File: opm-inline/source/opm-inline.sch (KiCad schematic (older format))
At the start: 0 parts

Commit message: more value updates
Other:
- note removed: "Release history:"
- note removed: "• v1.0 - First release.\n• v1.1 - shunt amplifier to the smaller type.\n signals to connector remapped: AIN0 = ADC_I_u and\n AIN1 = ADC_I_w.\n I_v signal removed.\n• v1.2 - Added pullup resistor for EPROM."
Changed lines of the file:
@@
 Comment4 ""
 $EndDescr
-Text Notes 500  650  0    79   ~ 0
-Release history:
-Text Notes 500  1050 0    39   ~ 0
-• v1.0 - First release.\n• v1.1 - shunt amplifier to the smaller type.\n          signals to connector remapped: AIN0 = ADC_I_u and\n          AIN1 = ADC_I_w.\n          I_v signal removed.\n• v1.2 - Added pullup resistor for EPROM.
-Wire Notes Line
-	500  500  500  1500
-Wire Notes Line
-	500  1500 2500 1500
 $Sheet
 S 5500 1000 1000 2000
@@
 Text Label 3400 1850 2    39   ~ 0
 VCP
-Wire Notes Line
-	2500 500  500  500
-Wire Notes Line
-	2500 1500 2500 500
 $EndSCHEMATC

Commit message: remove regulator
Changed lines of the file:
@@
 $Descr A4 11693 8268
 encoding utf-8
-Sheet 1 4
+Sheet 1 3
 Title "TMC6100-EVAL"
 Date "2019-10-28"
@@
 F26 "VCP" O R 6500 2300 39
 $EndSheet
-$Sheet
-S 7500 1000 1000 1000
-U 5D6A7BED
-F0 "Regulator and ID" 39
-F1 "Regulator and ID.sch" 39
-F2 "+5V_VM" I L 7500 1100 39
-F3 "+Vcc_IO" O R 8500 1100 39
-F4 "Fault" I L 7500 1200 39
-F5 "~CS_EEPROM" I L 7500 1300 39
-F6 "SPI2_SCK" I L 7500 1400 39
-F7 "SPI2_MOSI" I L 7500 1500 39
-F8 "SPI2_MISO" O R 8500 1200 39
-F9 "+3,3V" O R 8500 1300 39
-$EndSheet
-Text Label 8600 1100 0    39   ~ 0
-+Vcc_IO
-Wire Wire Line
-	8600 1100 8500 1100
-Wire Wire Line
-	8500 1200 8600 1200
-Wire Wire Line
-	7500 1100 7400 1100
-Wire Wire Line
-	7400 1200 7500 1200
-Wire Wire Line
-	7400 1300 7500 1300
-Wire Wire Line
-	7400 1400 7500 1400
-Wire Wire Line
-	7400 1500 7500 1500
 Wire Wire Line
 	6600 1100 6500 1100
@@
 Text Label 3400 1500 2    39   ~ 0
 +Vcc_IO
-Text Label 7400 1100 2    39   ~ 0
-+5V_VM
 Text Label 5400 1300 2    39   ~ 0
 +5V_VM
@@
 ADC_I_w
 Text Label 6600 1700 0    39   ~ 0
-Fault
-Text Label 7400 1200 2    39   ~ 0
 Fault
 Text Label 4600 1700 0    39   ~ 0
@@
 Text Label 3400 1300 2    39   ~ 0
 ADC_I_w
-Text Label 7400 1300 2    39   ~ 0
-~CS_EEPROM
 Text Label 4600 2800 0    39   ~ 0
 ~CS_EEPROM
@@
 Text Label 5400 1800 2    39   ~ 0
 SPI2_MOSI
-Text Label 7400 1500 2    39   ~ 0
-SPI2_MOSI
-Text Label 7400 1400 2    39   ~ 0
-SPI2_SCK
 Text Label 5400 1700 2    39   ~ 0
 SPI2_SCK
@@
 Text Label 6600 1800 0    39   ~ 0
 SPI2_MISO
-Text Label 8600 1200 0    39   ~ 0
-SPI2_MISO
 Text Label 4600 2700 0    39   ~ 0
 SPE
 Text Label 5400 1500 2    39   ~ 0
 SPE
-Wire Wire Line
-	8500 1300 8600 1300
-Text Label 8600 1300 0    39   ~ 0
-+3,3V
 $Sheet
 S 3500 1000 1000 2000

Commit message: fix connections
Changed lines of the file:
@@
 	4500 2700 4600 2700
-Wire Wire Line
-	4500 2800 4600 2800
 Wire Wire Line
 	3500 1100 3400 1100
@@
 Text Label 3400 1300 2    39   ~ 0
 ADC_I_w
-Text Label 4600 2800 0    39   ~ 0
-~CS_EEPROM
 Text Label 4600 2000 0    39   ~ 0
 ~CS_DRIVER
@@
 DRV_EN
 Text Label 4600 2200 0    39   ~ 0
-SPI2_MOSI
+SPI1_MOSI
 Text Label 5400 1800 2    39   ~ 0
 SPI2_MOSI
@@
 SPI2_SCK
 Text Label 4600 2300 0    39   ~ 0
-SPI2_SCK
+SPI1_SCK
 Text Label 3400 1400 2    39   ~ 0
-SPI2_MISO
+SPI1_MISO
 Text Label 6600 1800 0    39   ~ 0
 SPI2_MISO
@@
 F11 "WH" O R 4500 1900 39
 F12 "~CS_DRIVER" O R 4500 2000 39
-F13 "SPI2_MISO" I L 3500 1400 39
+F13 "SPI1_MISO" I L 3500 1400 39
 F14 "DRV_EN" O R 4500 2100 39
-F15 "SPI2_MOSI" O R 4500 2200 39
-F16 "SPI2_SCK" O R 4500 2300 39
+F15 "SPI1_MOSI" O R 4500 2200 39
+F16 "SPI1_SCK" O R 4500 2300 39
 F17 "WL" O R 4500 2600 39
 F18 "VL" O R 4500 2500 39
@@
 F21 "SPE" O R 4500 2700 39
 F22 "+Vcc_IO" I L 3500 1500 39
-F23 "~CS_EEPROM" O R 4500 2800 39
-F24 "VSA" I L 3500 1650 39
-F25 "12Vout" I L 3500 1750 39
-F26 "VCP" I L 3500 1850 39
-F27 "5Vout" I L 3500 1950 39
-F28 "+3,3V" I L 3500 2050 39
+F23 "VSA" I L 3500 1650 39
+F24 "12Vout" I L 3500 1750 39
+F25 "VCP" I L 3500 1850 39
+F26 "5Vout" I L 3500 1950 39
+F27 "+3,3V" I L 3500 2050 39
 $EndSheet
 Text Label 3400 2050 2    39   ~ 0

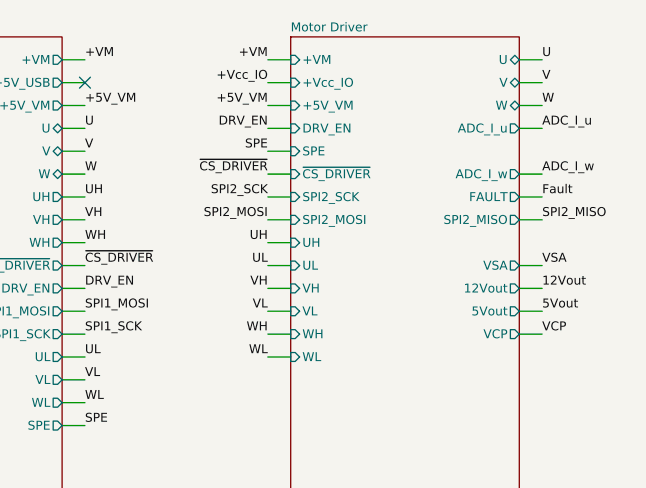
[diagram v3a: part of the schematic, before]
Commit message: adc out headers
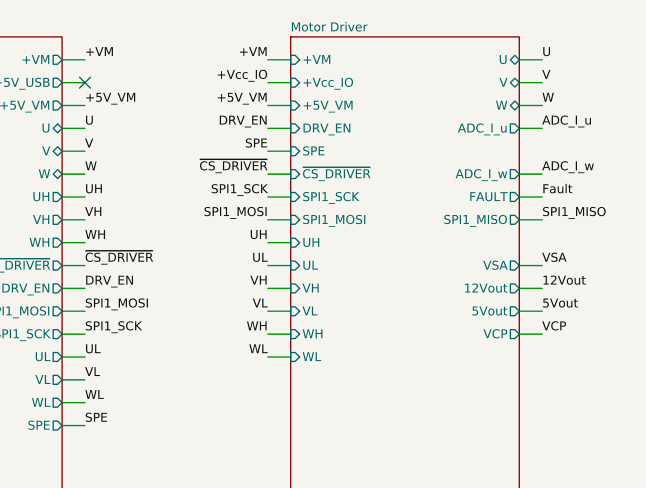
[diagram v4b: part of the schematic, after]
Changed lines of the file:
@@
 F6 "DRV_EN" I L 5500 1400 39
 F7 "SPE" I L 5500 1500 39
-F8 "SPI2_SCK" I L 5500 1700 39
-F9 "SPI2_MOSI" I L 5500 1800 39
-F10 "SPI2_MISO" O R 6500 1800 39
+F8 "SPI1_SCK" I L 5500 1700 39
+F9 "SPI1_MOSI" I L 5500 1800 39
+F10 "SPI1_MISO" O R 6500 1800 39
 F11 "UH" I L 5500 1900 39
 F12 "UL" I L 5500 2000 39
@@
 SPI1_MOSI
 Text Label 5400 1800 2    39   ~ 0
-SPI2_MOSI
+SPI1_MOSI
 Text Label 5400 1700 2    39   ~ 0
-SPI2_SCK
+SPI1_SCK
 Text Label 4600 2300 0    39   ~ 0
 SPI1_SCK
@@
 SPI1_MISO
 Text Label 6600 1800 0    39   ~ 0
-SPI2_MISO
+SPI1_MISO
 Text Label 4600 2700 0    39   ~ 0
 SPE

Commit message: add pcb
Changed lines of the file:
@@
 Text Label 5400 1500 2    39   ~ 0
 SPE
-$Sheet
-S 3500 1000 1000 2000
-U 5BA8C4E4
-F0 "Connevtors" 39
-F1 "Connevtors.sch" 39
-F2 "+VM" O R 4500 1100 39
-F3 "+5V_USB" O R 4500 1200 39
-F4 "+5V_VM" O R 4500 1300 39
-F5 "W" B R 4500 1600 39
-F6 "V" B R 4500 1500 39
-F7 "U" B R 4500 1400 39
-F8 "ADC_I_w" I L 3500 1300 39
-F9 "UH" O R 4500 1700 39
-F10 "VH" O R 4500 1800 39
-F11 "WH" O R 4500 1900 39
-F12 "~CS_DRIVER" O R 4500 2000 39
-F13 "SPI1_MISO" I L 3500 1400 39
-F14 "DRV_EN" O R 4500 2100 39
-F15 "SPI1_MOSI" O R 4500 2200 39
-F16 "SPI1_SCK" O R 4500 2300 39
-F17 "WL" O R 4500 2600 39
-F18 "VL" O R 4500 2500 39
-F19 "UL" O R 4500 2400 39
-F20 "ADC_I_u" I L 3500 1100 39
-F21 "SPE" O R 4500 2700 39
-F22 "+Vcc_IO" I L 3500 1500 39
-F23 "VSA" I L 3500 1650 39
-F24 "12Vout" I L 3500 1750 39
-F25 "VCP" I L 3500 1850 39
-F26 "5Vout" I L 3500 1950 39
-F27 "+3,3V" I L 3500 2050 39
-$EndSheet
 Text Label 3400 2050 2    39   ~ 0
 +3,3V
@@
 Text Label 3400 1850 2    39   ~ 0
 VCP
+Wire Wire Line
+	3500 1200 3400 1200
+Text Label 3400 1200 2    39   ~ 0
+ADC_I_v
+$Sheet
+S 3500 1000 1000 2000
+U 5BA8C4E4
+F0 "Connevtors" 39
+F1 "Connevtors.sch" 39
+F2 "+VM" O R 4500 1100 39
+F3 "+5V_USB" O R 4500 1200 39
+F4 "+5V_VM" O R 4500 1300 39
+F5 "W" B R 4500 1600 39
+F6 "V" B R 4500 1500 39
+F7 "U" B R 4500 1400 39
+F8 "ADC_I_w" I L 3500 1300 39
+F9 "UH" O R 4500 1700 39
+F10 "VH" O R 4500 1800 39
+F11 "WH" O R 4500 1900 39
+F12 "~CS_DRIVER" O R 4500 2000 39
+F13 "SPI1_MISO" I L 3500 1400 39
+F14 "DRV_EN" O R 4500 2100 39
+F15 "SPI1_MOSI" O R 4500 2200 39
+F16 "SPI1_SCK" O R 4500 2300 39
+F17 "WL" O R 4500 2600 39
+F18 "VL" O R 4500 2500 39
+F19 "UL" O R 4500 2400 39
+F20 "ADC_I_u" I L 3500 1100 39
+F21 "SPE" O R 4500 2700 39
+F22 "+Vcc_IO" I L 3500 1500 39
+F23 "VSA" I L 3500 1650 39
+F24 "12Vout" I L 3500 1750 39
+F25 "VCP" I L 3500 1850 39
+F26 "5Vout" I L 3500 1950 39
+F27 "+3,3V" I L 3500 2050 39
+F28 "ADC_I_v" I L 3500 1200 39
+F29 "VCC" I L 3500 2550 28
+$EndSheet
 $EndSCHEMATC
